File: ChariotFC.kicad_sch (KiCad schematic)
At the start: 47 parts, among them SW1 1TS009A-1800-5000, SW2 1TS009A-1800-5000, U1 TLV75733PDRVR, U2 FM25V20A-DGTR_C2952834, U4 NCP167BMX330TBG, U5 USBLC6-2SC6Y_C2969755, U7 AT32F435RMT7, U9 B6B-XH-A(LF)(SN), X1 ABM3-8.000MHZ-D2Y-T

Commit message: GPS connections made
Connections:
- net CURRENT_SCALED: now also U7.16 (PA2)
- net VBAT_SCALED: now also U7.15 (PA1)
- net nRST renamed ~{RST}
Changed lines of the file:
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@@
 		(effects
 			(font
-				(size 0.762 0.762)
+				(size 1.778 1.778)
+				(thickness 0.3556)
+				(bold yes)
 			)
 		)
@@
 	(text "Takes 5v from PDB connector and USB-C \nand lets one of them pass through."
 		(exclude_from_sim no)
-		(at 262.382 70.866 0)
+		(at 263.398 72.898 0)
 		(effects
 			(font
@@
 		(effects
 			(font
-				(size 0.762 0.762)
+				(size 1.778 1.778)
+				(thickness 0.3556)
+				(bold yes)
 			)
 		)
@@
 		(effects
 			(font
-				(size 0.762 0.762)
+				(size 1.778 1.778)
+				(thickness 0.3556)
+				(bold yes)
 			)
 		)
@@
 		(effects
 			(font
-				(size 0.762 0.762)
+				(size 1.778 1.778)
+				(thickness 0.3556)
+				(bold yes)
 			)
 		)
@@
 		(effects
 			(font
-				(size 0.762 0.762)
+				(size 1.778 1.778)
+				(thickness 0.3556)
+				(bold yes)
 			)
 		)
@@
 		(effects
 			(font
-				(size 0.762 0.762)
+				(size 1.778 1.778)
+				(thickness 0.3556)
+				(bold yes)
 			)
 		)
@@
 	(wire
 		(pts
-			(xy 165.1 97.79) (xy 166.37 97.79)
-		)
-		(stroke
-			(width 0)
-			(type default)
-		)
-	)
-	(wire
-		(pts
 			(xy 198.12 35.56) (xy 201.93 35.56)
 		)
@@
 	(wire
 		(pts
-			(xy 165.1 125.73) (xy 166.37 125.73)
-		)
-		(stroke
-			(width 0)
-			(type default)
-		)
-	)
-	(wire
-		(pts
 			(xy 107.95 95.25) (xy 110.49 95.25)
 		)
@@
 	(wire
 		(pts
-			(xy 165.1 90.17) (xy 166.37 90.17)
-		)
-		(stroke
-			(width 0)
-			(type default)
-		)
-	)
-	(wire
-		(pts
 			(xy 55.88 134.62) (xy 71.12 134.62)
 		)
@@
 	(wire
 		(pts
-			(xy 165.1 95.25) (xy 166.37 95.25)
-		)
-		(stroke
-			(width 0)
-			(type default)
-		)
-	)
-	(wire
-		(pts
 			(xy 130.81 180.34) (xy 140.97 180.34)
 		)
@@
 	(wire
 		(pts
-			(xy 165.1 123.19) (xy 166.37 123.19)
-		)
-		(stroke
-			(width 0)
-			(type default)
-		)
-	)
-	(wire
-		(pts
 			(xy 196.85 110.49) (xy 201.93 110.49)
 		)
@@
 	(wire
 		(pts
-			(xy 165.1 128.27) (xy 166.37 128.27)
-		)
-		(stroke
-			(width 0)
-			(type default)
-		)
-	)
-	(wire
-		(pts
 			(xy 209.55 78.74) (xy 209.55 77.47)
 		)
@@
 	(wire
 		(pts
-			(xy 165.1 92.71) (xy 166.37 92.71)
-		)
-		(stroke
-			(width 0)
-			(type default)
-		)
-	)
-	(wire
-		(pts
 			(xy 110.49 85.09) (xy 115.57 85.09)
 		)
@@
 	(global_label "SDIO_D1"
 		(shape input)
-		(at 166.37 125.73 0)
+		(at 165.1 125.73 0)
 		(fields_autoplaced yes)
 		(effects
@@
 		)
 		(property "Intersheetrefs" "${INTERSHEET_REFS}"
-			(at 172.8786 125.73 0)
+			(at 171.6086 125.73 0)
 			(effects
 				(font
@@
 	(global_label "CURRENT_SCALED"
 		(shape input)
-		(at 168.91 49.53 180)
+		(at 129.54 102.87 180)
 		(fields_autoplaced yes)
 		(effects
@@
 		)
 		(property "Intersheetrefs" "${INTERSHEET_REFS}"
-			(at 157.1763 49.53 0)
+			(at 117.8063 102.87 0)
 			(effects
 				(font
@@
 	(global_label "SDIO_CD"
 		(shape input)
-		(at 166.37 123.19 0)
+		(at 165.1 123.19 0)
 		(fields_autoplaced yes)
 		(effects
@@
 		)
 		(property "Intersheetrefs" "${INTERSHEET_REFS}"
-			(at 172.9149 123.19 0)
+			(at 171.6449 123.19 0)
 			(effects
 				(font
@@
 	(global_label "SDIO_D0"
 		(shape input)
-		(at 166.37 128.27 0)
+		(at 165.1 128.27 0)
 		(fields_autoplaced yes)
 		(effects
@@
 		)
 		(property "Intersheetrefs" "${INTERSHEET_REFS}"
-			(at 172.8786 128.27 0)
+			(at 171.6086 128.27 0)
 			(effects
 				(font
@@
 	(global_label "SDIO_CLK"
 		(shape input)
-		(at 166.37 92.71 0)
+		(at 165.1 92.71 0)
 		(fields_autoplaced yes)
 		(effects
@@
 		)
 		(property "Intersheetrefs" "${INTERSHEET_REFS}"
-			(at 173.5318 92.71 0)
+			(at 172.2618 92.71 0)
 			(effects
 				(font
@@
 	(global_label "VBAT_SCALED"
 		(shape input)
-		(at 166.37 53.34 180)
+		(at 129.54 100.33 180)
 		(fields_autoplaced yes)
 		(effects
@@
 		)
 		(property "Intersheetrefs" "${INTERSHEET_REFS}"
-			(at 157.1401 53.34 0)
+			(at 120.3101 100.33 0)
 			(effects
 				(font
@@
 		)
 	)
+	(global_label "~{RST}"
+		(shape input)
+		(at 129.54 72.39 180)
+		(fields_autoplaced yes)
+		(effects
+			(font
+				(size 0.762 0.762)
+			)
+			(justify right)
+		)
+		(property "Intersheetrefs" "${INTERSHEET_REFS}"
+			(at 121.8218 72.39 0)
+			(effects
+				(font
+					(size 0.762 0.762)
+				)
+				(justify right)
+				(hide yes)
+			)
+		)
+	)
 	(global_label "SDIO_CMD"
 		(shape input)
-		(at 166.37 90.17 0)
+		(at 165.1 90.17 0)
 		(fields_autoplaced yes)
 		(effects
@@
 		)
 		(property "Intersheetrefs" "${INTERSHEET_REFS}"
-			(at 173.7858 90.17 0)
+			(at 172.5158 90.17 0)
 			(effects
 				(font
@@
 	(global_label "SDIO_D2"
 		(shape input)
-		(at 166.37 97.79 0)
+		(at 165.1 97.79 0)
 		(fields_autoplaced yes)
 		(effects
@@
 		)
 		(property "Intersheetrefs" "${INTERSHEET_REFS}"
-			(at 172.8786 97.79 0)
+			(at 171.6086 97.79 0)
 			(effects
 				(font
@@
 	(global_label "SDIO_D3"
 		(shape input)
-		(at 166.37 95.25 0)
+		(at 165.1 95.25 0)
 		(fields_autoplaced yes)
 		(effects
@@
 		)
 		(property "Intersheetrefs" "${INTERSHEET_REFS}"
-			(at 172.8786 95.25 0)
+			(at 171.6086 95.25 0)
 			(effects
 				(font
@@
 		)
 	)
-	(global_label "nRST"
-		(shape input)
-		(at 129.54 72.39 180)
-		(fields_autoplaced yes)
-		(effects
-			(font
-				(size 0.762 0.762)
-			)
-			(justify right)
-		)
-		(property "Intersheetrefs" "${INTERSHEET_REFS}"
-			(at 124.2332 72.39 0)
-			(effects
-				(font
-					(size 0.762 0.762)
-				)
-				(justify right)
-				(hide yes)
-			)
-		)
-	)
-	(global_label "nRST"
+	(global_label "~{RST}"
 		(shape input)
 		(at 26.67 40.64 180)
@@
 		)
 		(property "Intersheetrefs" "${INTERSHEET_REFS}"
-			(at 21.3632 40.64 0)
+			(at 18.9518 40.64 0)
 			(effects
 				(font
@@
 			(effects
 				(font
-					(size 1.27 1.27)
+					(size 0.762 0.762)
 				)
 			)
@@
 			(effects
 				(font
-					(size 1.27 1.27)
+					(size 0.762 0.762)
 				)
 			)
@@
 			(effects
 				(font
-					(size 1.27 1.27)
+					(size 0.762 0.762)
 				)
 				(hide yes)
@@
 			(effects
 				(font
-					(size 1.27 1.27)
+					(size 0.762 0.762)
 				)
 				(hide yes)
@@
 			(effects
 				(font
-					(size 1.27 1.27)
+					(size 0.762 0.762)
 				)
 				(hide yes)
@@
 			(effects
 				(font
-					(size 1.27 1.27)
+					(size 0.762 0.762)
 				)
 				(hide yes)
@@
 		(on_board yes)
 		(dnp no)
-		(fields_autoplaced yes)
 		(property "Reference" "#FLG03"
 			(at 119.38 97.155 0)
@@
 		)
 		(property "Value" "PWR_FLAG"
-			(at 119.38 100.33 0)
+			(at 117.094 98.806 0)
 			(effects
 				(font
@@
 			(effects
 				(font
-					(size 1.27 1.27)
+					(size 0.762 0.762)
 				)
 			)
@@
 			(effects
 				(font
-					(size 1.27 1.27)
+					(size 0.762 0.762)
 				)
 			)
@@
 			(effects
 				(font
-					(size 1.27 1.27)
+					(size 0.762 0.762)
 				)
 				(hide yes)
@@
 			(effects
 				(font
-					(size 1.27 1.27)
+					(size 0.762 0.762)
 				)
 				(hide yes)
@@
 			(effects
 				(font
-					(size 1.27 1.27)
+					(size 0.762 0.762)
 				)
 				(hide yes)
@@
 			(effects
 				(font
-					(size 1.27 1.27)
+					(size 0.762 0.762)
 				)
 				(hide yes)

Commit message: Cleaned up circuit
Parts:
- added C40: 100nF, easyeda2kicad:C0402, symbol easyeda2kicad:CL05B104KO5NNNC
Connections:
- net +3V3: now also U7.1 (VBAT), C40.1
- net GND: now also U7.18 (VSS), U7.63 (VSS), C40.2
- net ~{RST}: now also U7.7 (NRST); no longer U7.4 (PC15)

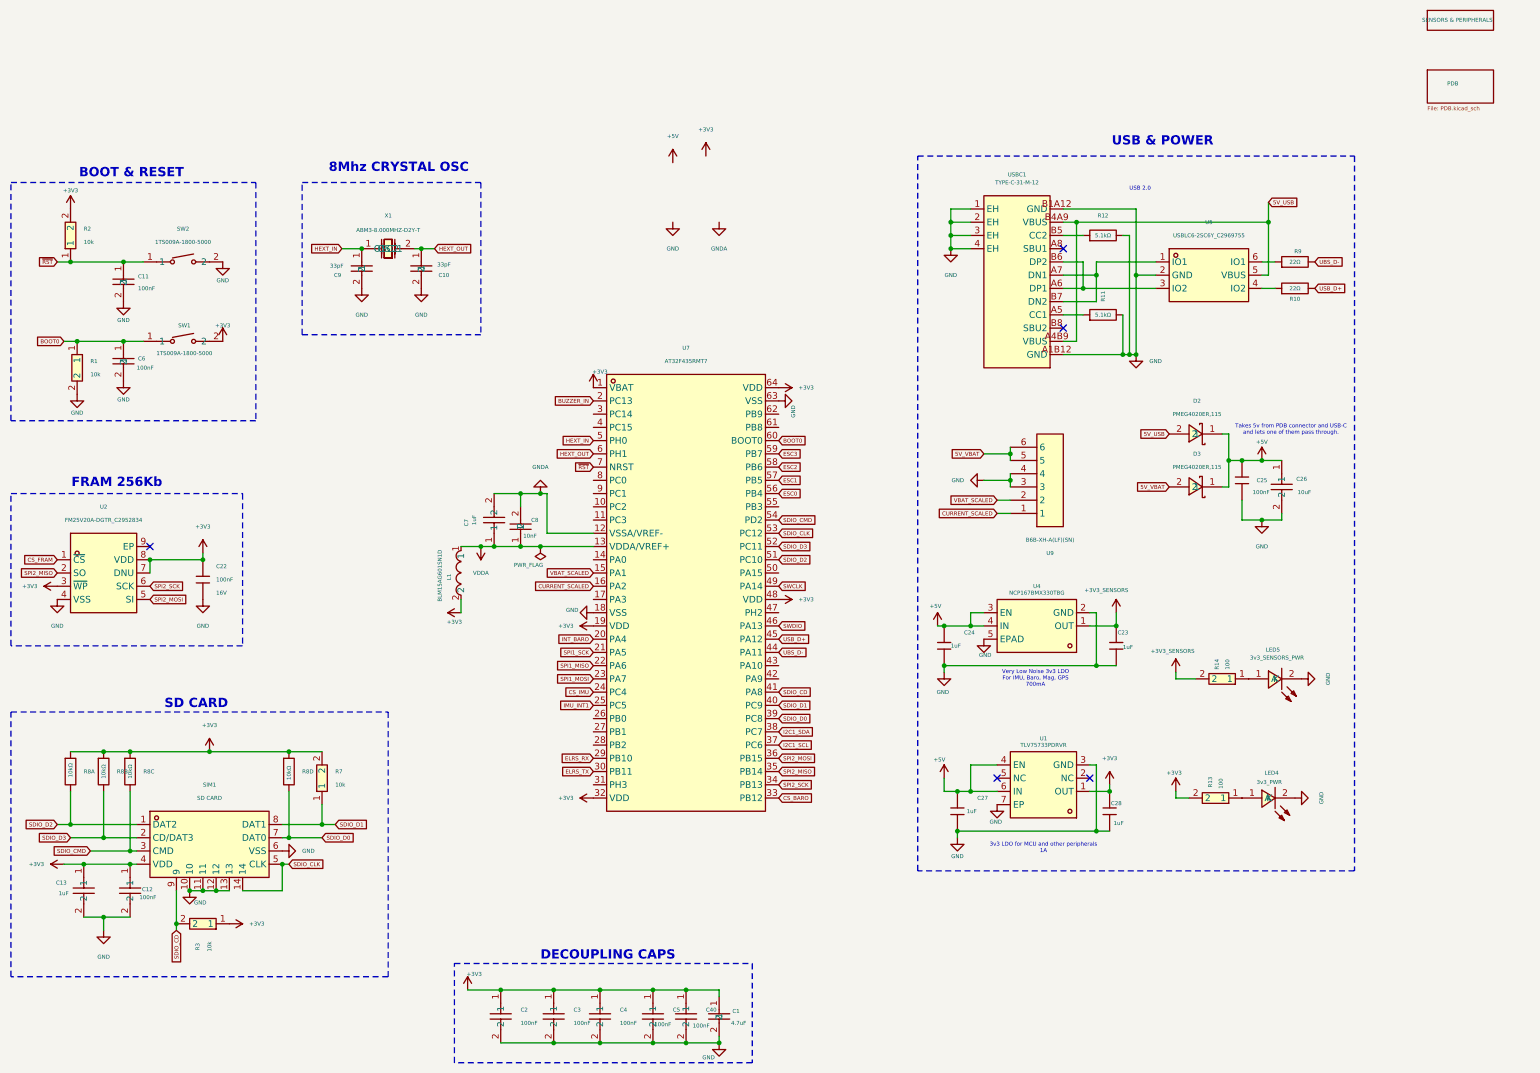
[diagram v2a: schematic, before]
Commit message: Added PWR flags, Changed MCU pins electrical characteristics to bidirectional, rectified some ERC errors
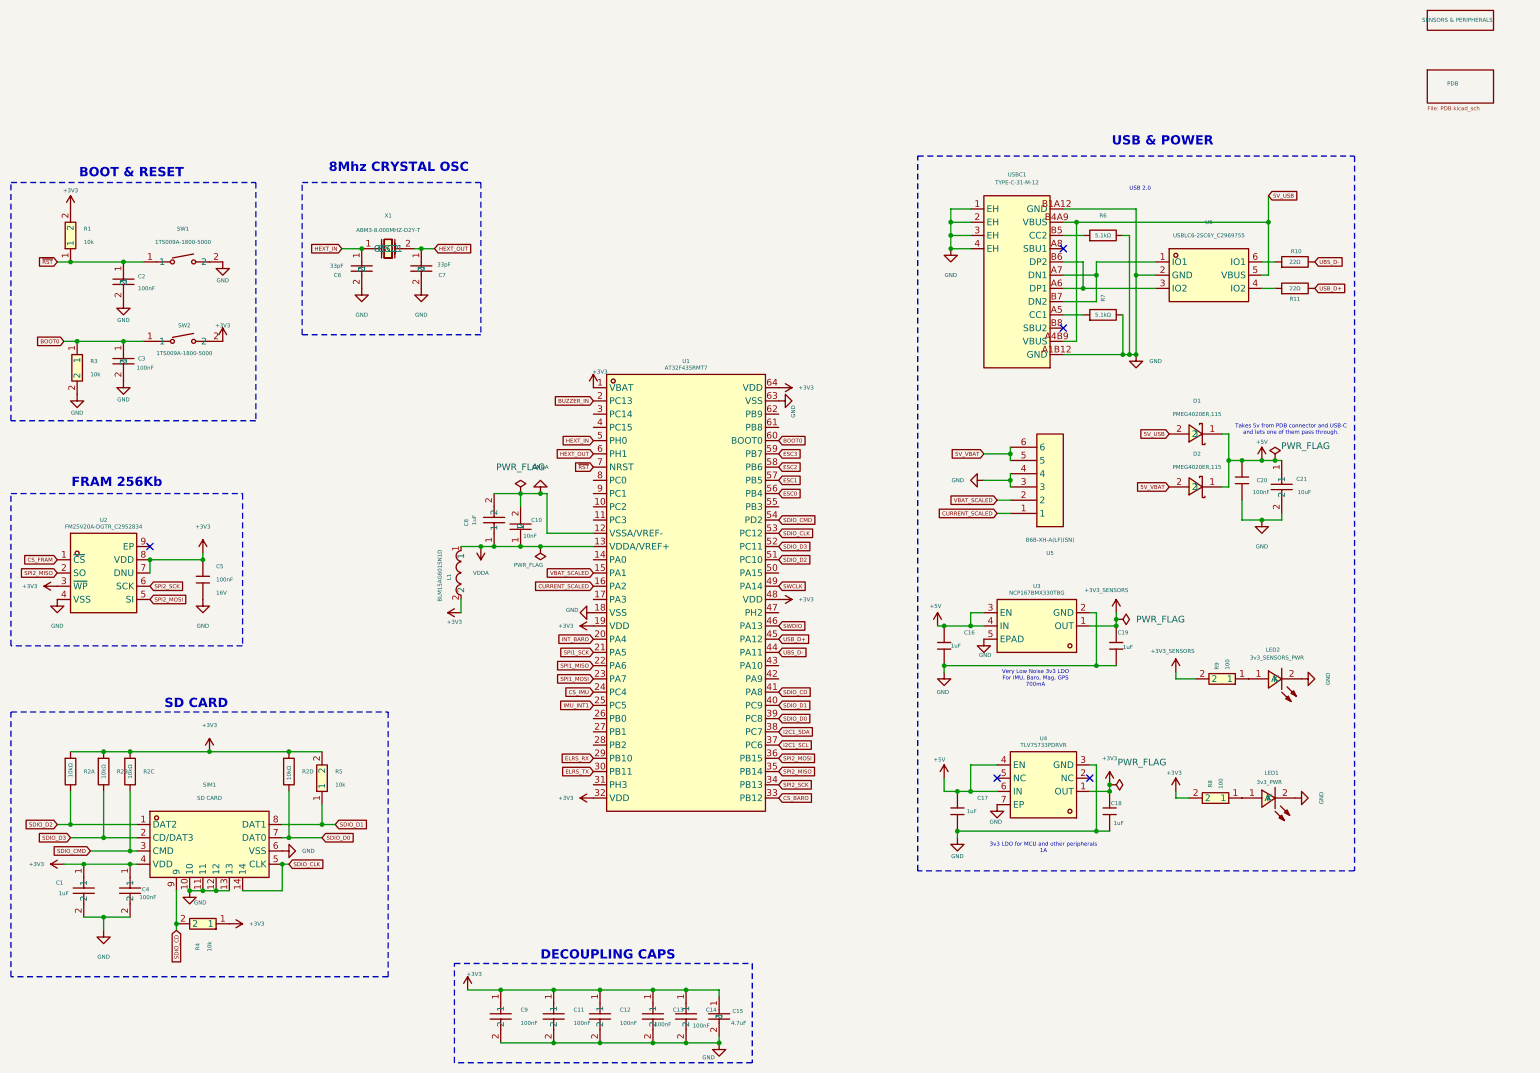
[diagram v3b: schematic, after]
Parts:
- renumbered C13 to C1, C8 to C10, C3 to C11, C4 to C12, C5 to C13, C40 to C14, C1 to C15, C24 to C16, C27 to C17, C28 to C18, C23 to C19, C11 to C2, C25 to C20, C26 to C21, C6 to C3, C12 to C4, C22 to C5, C9 to C6, C10 to C7, C7 to C8, C2 to C9, D2 to D1, D3 to D2, LED4 to LED1, LED5 to LED2, R2 to R1, R9 to R10, R10 to R11, R8 to R2, R1 to R3, R3 to R4, R7 to R5, R12 to R6, R11 to R7, R13 to R8, R14 to R9, SW2 to SW1, SW1 to SW2, U7 to U1, U4 to U3, U1 to U4, U9 to U5, U5 to U6

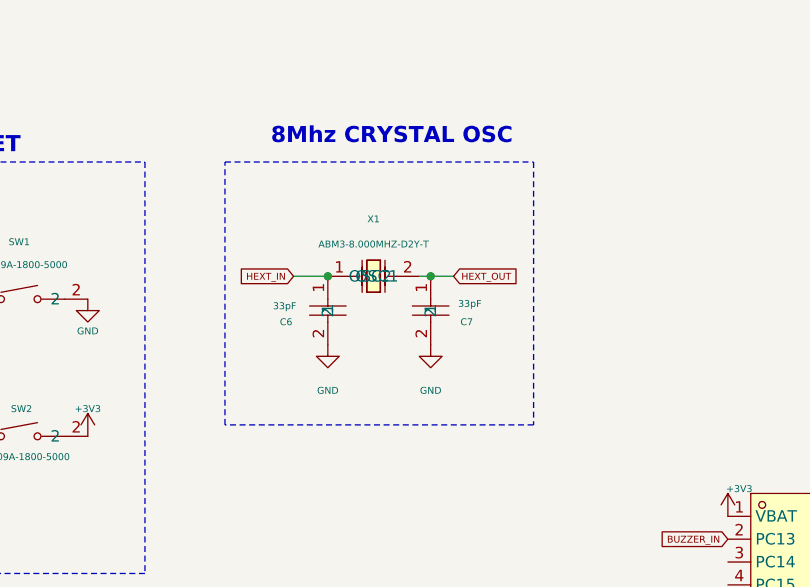
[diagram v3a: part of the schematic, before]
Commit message: Put the orrect load capacitances fo the External Osc
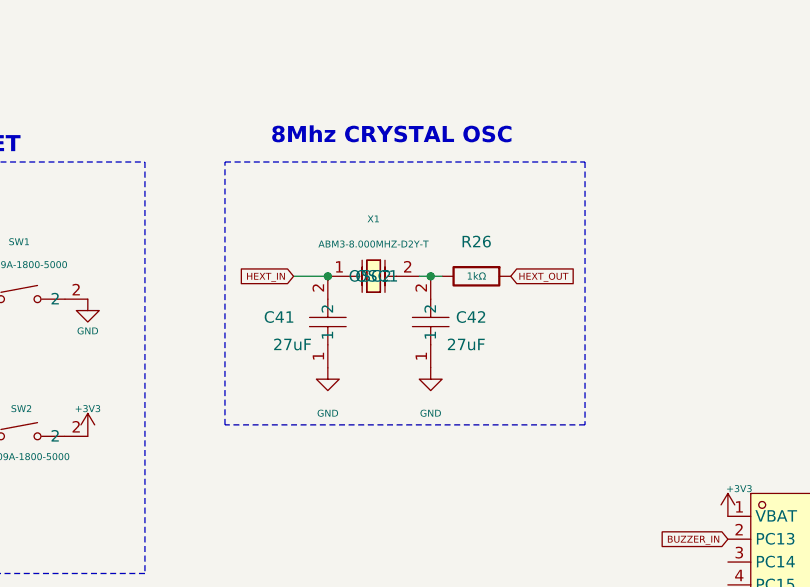
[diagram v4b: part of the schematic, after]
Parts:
- removed C6, C7: 33pF, easyeda2kicad:C0402, symbol easyeda2kicad:0402CG330J500NT
- added C41, C42: 27uF, easyeda2kicad:C0402, symbol easyeda2kicad:C1005C0G1H270JT000F
- added R26: 1kΩ, PCM_JLCPCB:R_0402, symbol PCM_JLCPCB-Resistors:0402,1kΩ
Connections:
- net GND: now also C41.1, C42.1
- net HEXT_IN: now also C41.2
- net HEXT_OUT: now also R26.1; no longer X1.2 (OSC2)
- new net: C42.2, R26.2, X1.2 (OSC2)
